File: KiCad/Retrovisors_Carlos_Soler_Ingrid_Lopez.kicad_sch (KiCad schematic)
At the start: 0 parts

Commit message: Inici kiCat
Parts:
- added U1: LM74700, Package_TO_SOT_SMD:SOT-23-6, symbol Power_Management:LM74700
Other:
- note added: "Potencia"
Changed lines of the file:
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@@
 	(generator_version "9.0")
 	(paper "A4")
+	(text "Potencia\n"
+		(exclude_from_sim no)
+		(at 55.88 21.082 0)
+		(effects
+			(font
+				(size 5.08 5.08)
+			)
+		)
+	)
+	(symbol
+		(lib_id "Power_Management:LM74700")
+		(at 59.69 46.99 0)
+		(unit 1)
+		(exclude_from_sim no)
+		(in_bom yes)
+		(on_board yes)
+		(dnp no)
+		(fields_autoplaced yes)
+		(property "Reference" "U1"
+			(at 71.12 45.7199 0)
+			(effects
+				(font
+					(size 1.27 1.27)
+				)
+				(justify left)
+			)
+		)
+		(property "Value" "LM74700"
+			(at 71.12 48.2599 0)
+			(effects
+				(font
+					(size 1.27 1.27)
+				)
+				(justify left)
+			)
+		)
+		(property "Footprint" "Package_TO_SOT_SMD:SOT-23-6"
+			(at 50.165 55.88 0)
+			(effects
+				(font
+					(size 1.27 1.27)
+				)
+				(hide yes)
+			)
+		)
+		(property "Datasheet" "http://www.ti.com/lit/gpn/LM74700-Q1"
+			(at 50.165 55.88 0)
+			(effects
+				(font
+					(size 1.27 1.27)
+				)
+				(hide yes)
+			)
+		)
+		(property "Description" "Low Iq reverse battery protection ideal diode controller, SOT-23-6"
+			(at 59.69 46.99 0)
+			(effects
+				(font
+					(size 1.27 1.27)
+				)
+				(hide yes)
+			)
+		)
+		(pin "1"
+		)
+		(pin "6"
+		)
+		(pin "2"
+		)
+		(pin "4"
+		)
+		(pin "5"
+		)
+		(pin "3"
+		)
+		(instances
+			(project ""
+				(path "/a9cf8edd-cd44-4958-b775-951afc8c27af"
+					(reference "U1")
+					(unit 1)
+				)
+			)
+		)
+	)
 	(sheet_instances
 		(path "/"

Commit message: Etapa de alimentació 1
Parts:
- removed U1: LM74700, Package_TO_SOT_SMD:SOT-23-6, symbol Power_Management:LM74700
- added D1: D, symbol Device:D
- added D2: D_transil, symbol Device:D_Zener
- added J1: Conn_01x02, symbol Connector_Generic:Conn_01x02
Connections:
- new net: D1.2 (A), J1.1 (Pin_1)
- new net: D1.1 (K), D2.1 (K)
- new net GNDPWR: D2.2 (A), J1.2 (Pin_2)
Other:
- note added: "Alimentació"
- note removed: "Potencia"

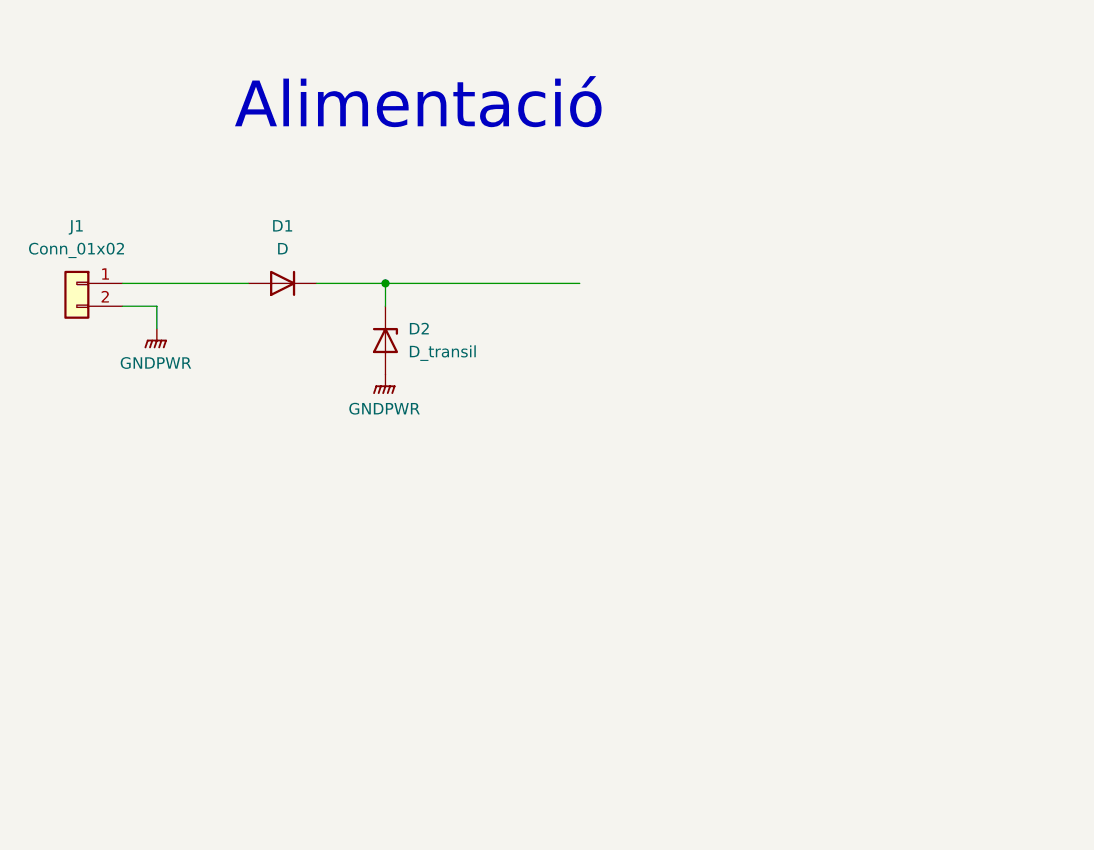
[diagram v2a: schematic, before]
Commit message: Etapa de alimentacio completa
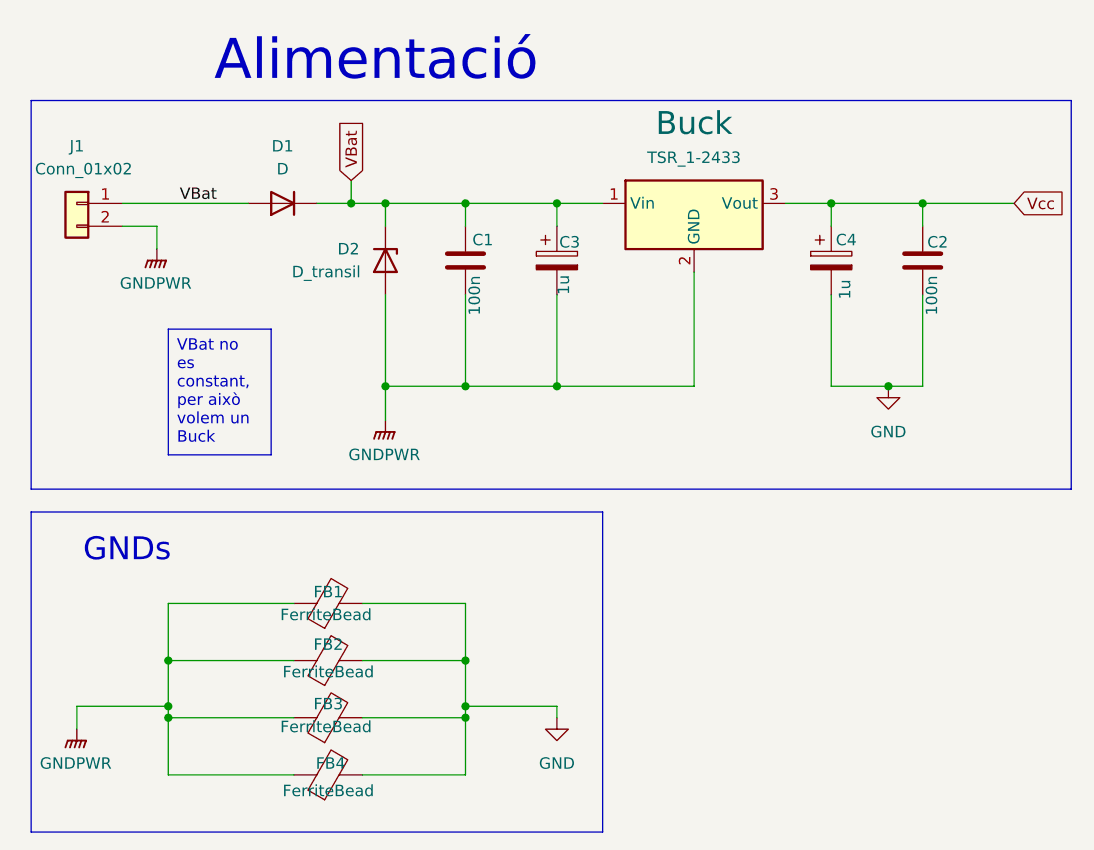
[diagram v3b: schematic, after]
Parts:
- added Buck: TSR_1-2433, Converter_DCDC:Converter_DCDC_TRACO_TSR-1_THT, symbol Converter_DCDC:TSR_1-2433
- added C1, C2: 100n, symbol Device:C
- added C3, C4: 1u, symbol Device:C_Polarized
- added FB1, FB2, FB3, FB4: FerriteBead, symbol Device:FerriteBead
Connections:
- net GNDPWR: now also Buck.2 (GND), C1.2, C3.2, FB1.1, FB2.1, FB3.1, FB4.1
- net VBat: now reaches D1.2 (A), J1.1 (Pin_1)
- net VBat: now also D1.1 (K), D2.1 (K), Buck.1 (Vin), C1.1, C3.1
- new net GND: C2.2, C4.2, FB1.2, FB2.2, FB3.2, FB4.2
- new net Vcc: Buck.3 (Vout), C2.1, C4.1
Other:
- note added: "GNDs"
- moved on the sheet: D1, D2, J1

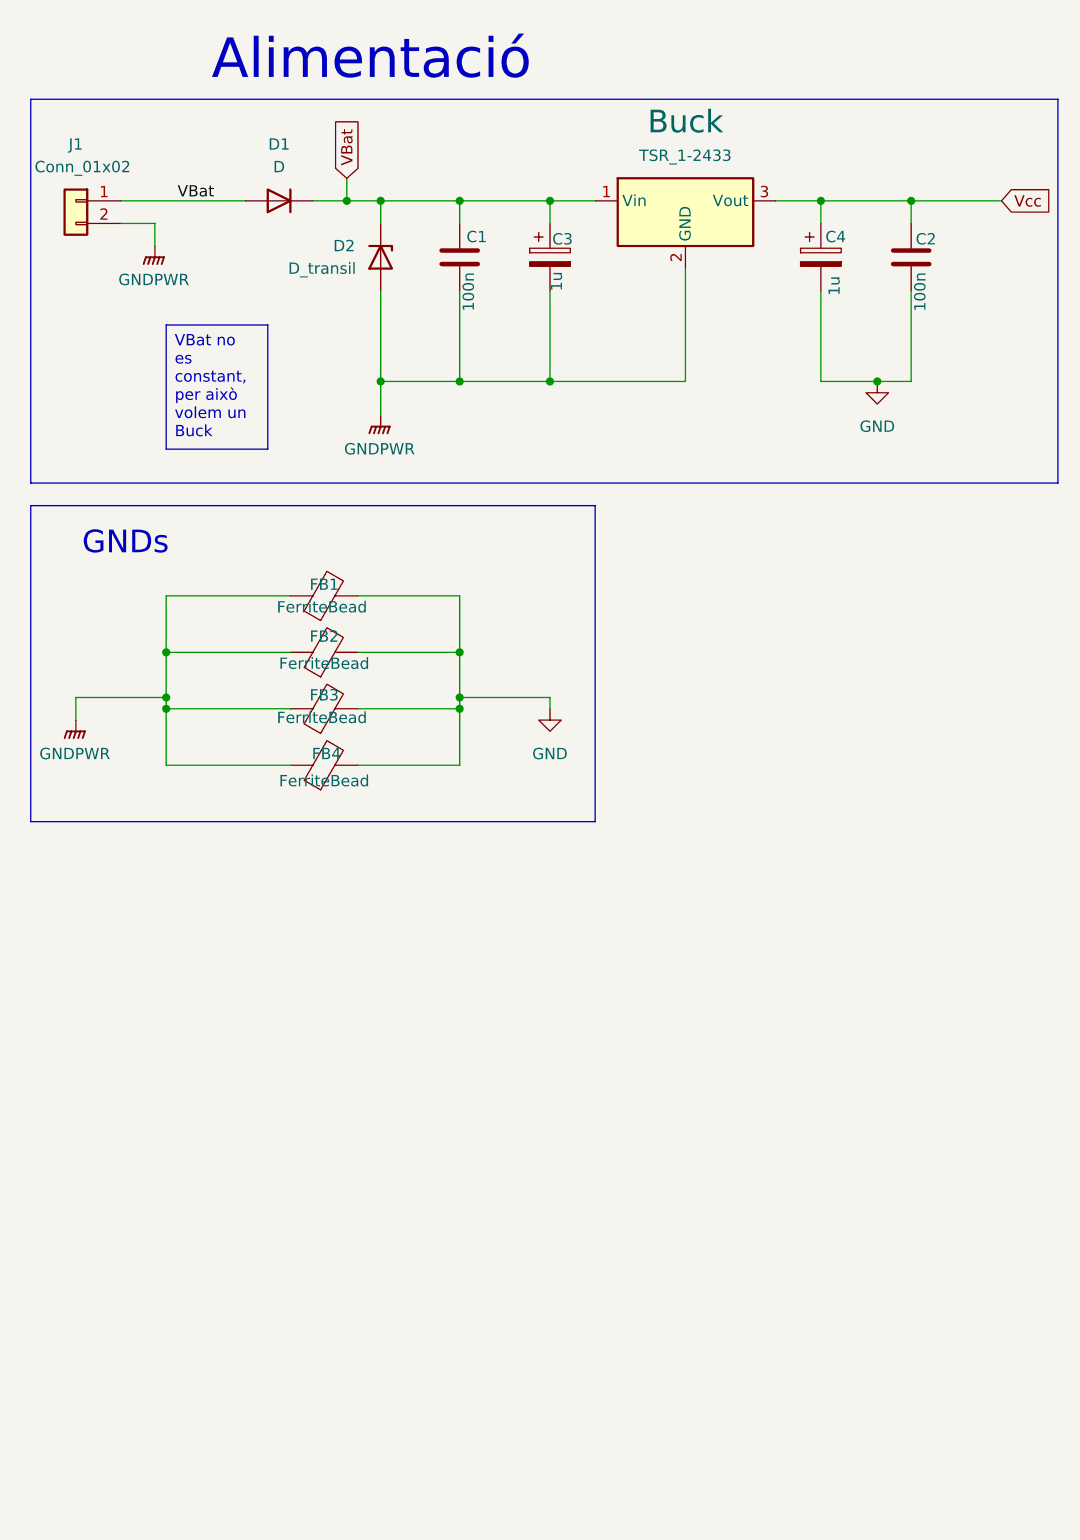
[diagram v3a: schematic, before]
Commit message: Alimentacio finalitzada e inici de micro
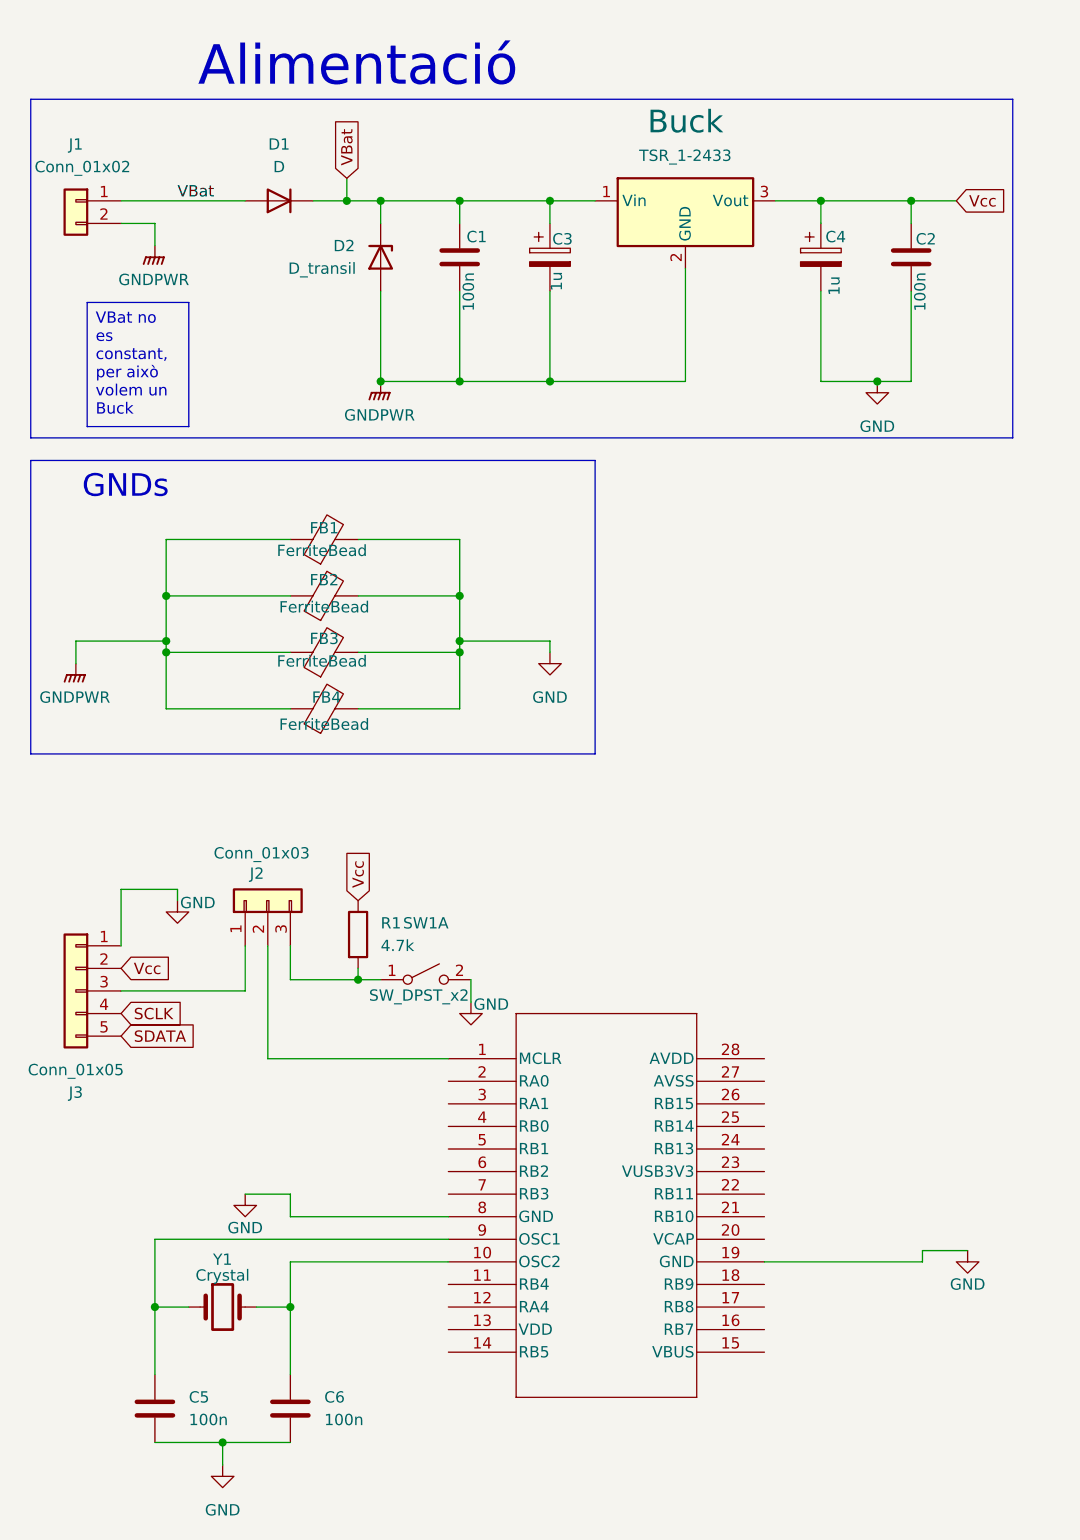
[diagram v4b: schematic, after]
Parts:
- added C5, C6: 100n, symbol Device:C
- added J2: Conn_01x03, symbol Connector_Generic:Conn_01x03
- added J3: Conn_01x05, symbol Connector_Generic:Conn_01x05
- added R1: 4.7k, symbol Device:R
- added SW1: SW_DPST_x2, symbol Switch:SW_DPST_x2
- added U1: PIC32MX250F128B-50I/SO, SOIC28-W_MC_MCH, symbol PIC32MX250F128B_50I_SO:PIC32MX250F128B-50I_SO
- added Y1: Crystal, symbol Device:Crystal
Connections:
- net GND: now also C5.2, C6.2, J3.1 (Pin_1), SW1.2 (B), U1.19 (GND), U1.8 (GND)
- net Vcc: now also J3.2 (Pin_2), R1.1
- new net: C6.1, U1.10 (OSC2), Y1.2
- new net: J2.3 (Pin_3), R1.2, SW1.1 (A)
- new net: J2.1 (Pin_1), J3.3 (Pin_3)
- new net: C5.1, U1.9 (OSC1), Y1.1
- new net: J2.2 (Pin_2), U1.1 (MCLR)
- new net SCLK: J3.4 (Pin_4)
- new net SDATA: J3.5 (Pin_5)
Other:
- moved on the sheet: FB1, FB2, FB3, FB4

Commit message: microcontrolador i driver
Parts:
- added J4: Conn_01x08, symbol Connector_Generic:Conn_01x08
- added U2: DRV8906QPWPRQ1, HTSSOP24_PWP_TEX, symbol Drivers_motors_xy:DRV8906QPWPRQ1
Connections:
- net GND: now also U2.1 (GND), U2.13 (GND), U2.24 (GND), U2.EPAD (GND)
- net SCLK: now also U1.25 (RB14), U2.20 (SCLK)
- net Vcc: now also U1.13 (VDD), U2.6 (VDD)
- net nSLEEP: now reaches U1.17 (RB8)
- net nSLEEP: now also U2.8 (NSLEEP)
- net nSCS: now reaches U1.18 (RB9)
- net nSCS: now also U2.19 (NSCS)
- net SDI2: now reaches U1.21 (RB10)
- net SDI2: now also U2.7 (SDO)
- net SDO2: now reaches U1.22 (RB11)
- net SDO2: now also U2.5 (SDI)
- new net Motor1_I1: U2.2 (OUT1)
- new net Motor1_I2: U2.23 (OUT2)
- new net Motor2_I1: U2.14 (OUT3)
- new net Motor2_I2: U2.11 (OUT4)
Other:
- note added: "Microcontrolador"
- moved on the sheet: C5, C6, J2, J3, R1, SW1A, Y1
